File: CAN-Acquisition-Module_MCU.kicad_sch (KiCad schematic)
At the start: 23 parts

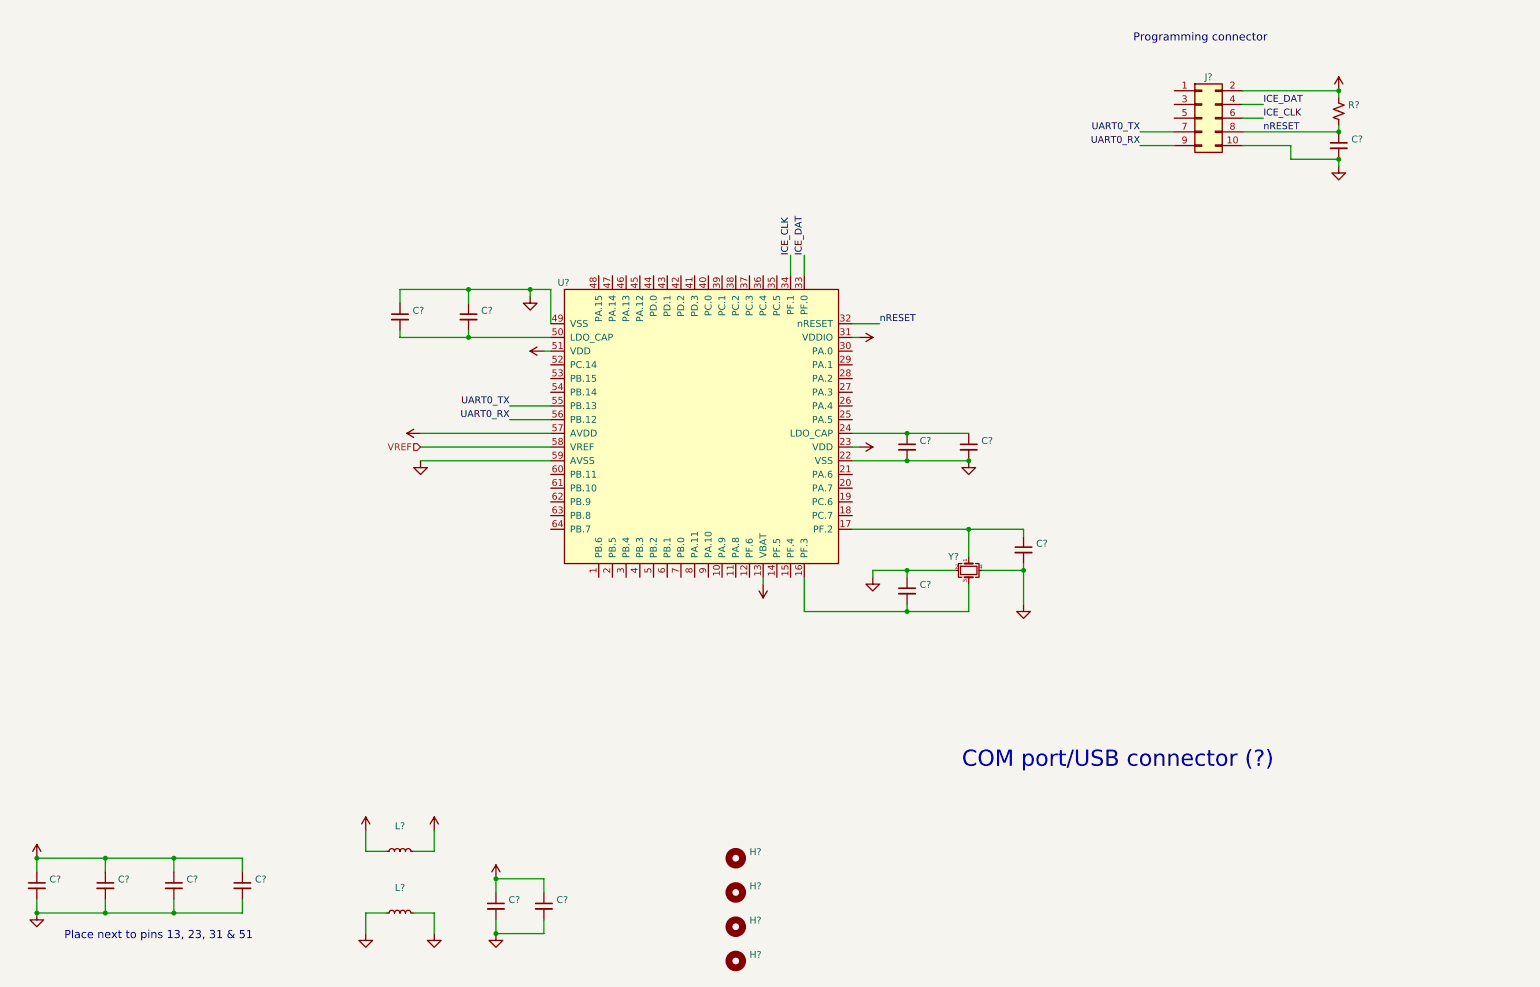
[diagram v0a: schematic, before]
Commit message: Added CAN page
also power section has advanced
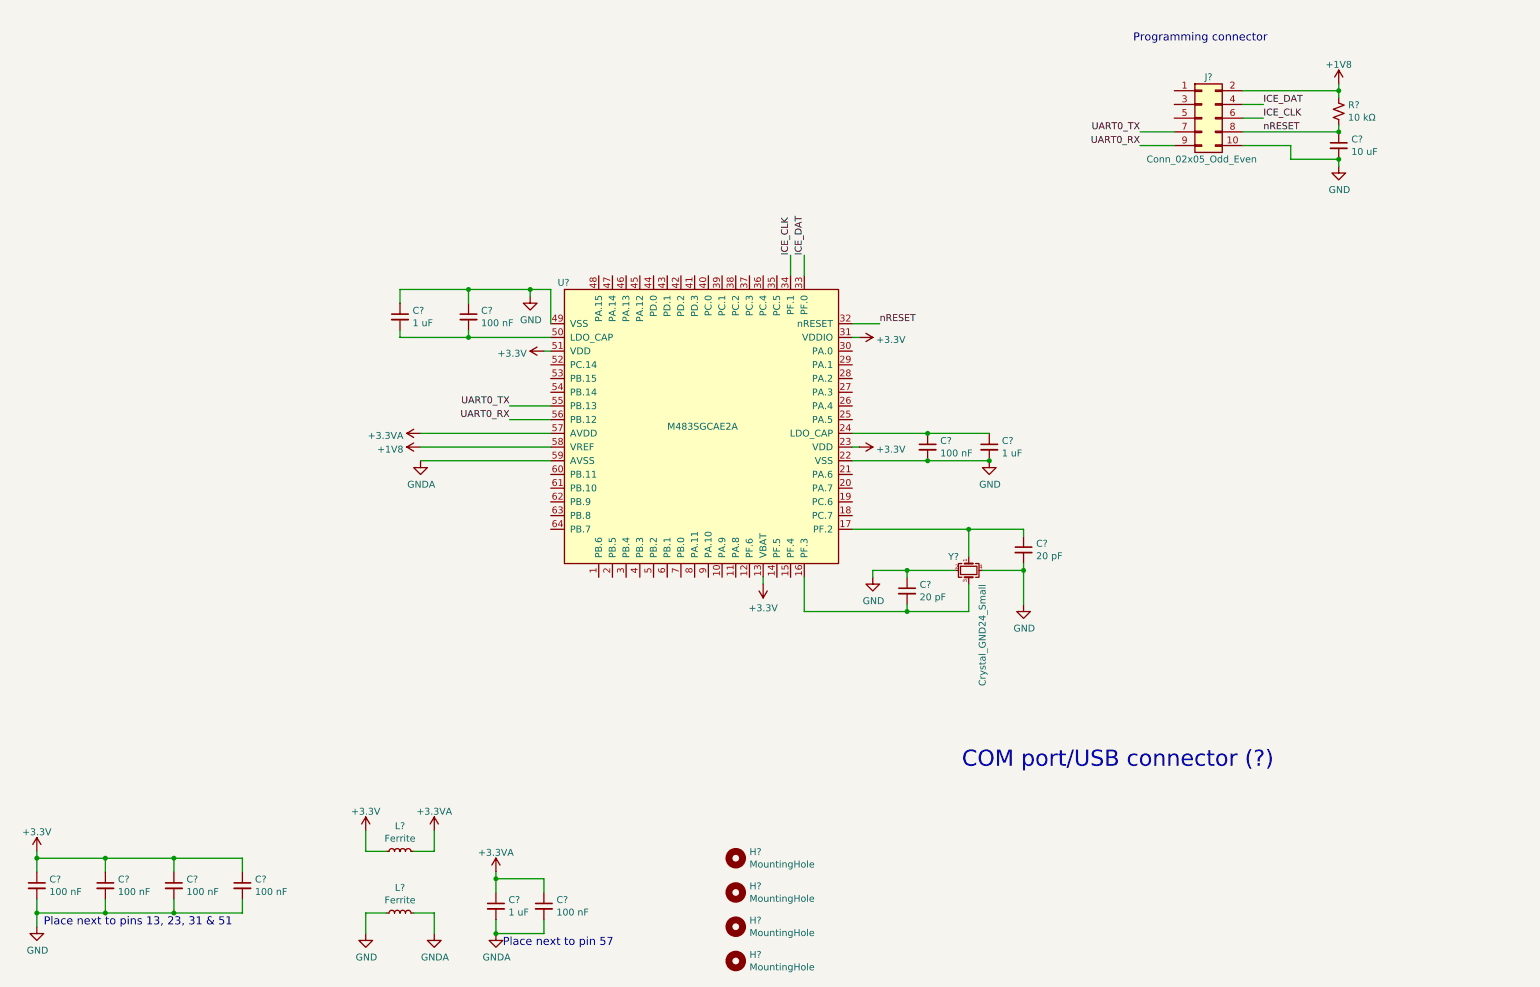
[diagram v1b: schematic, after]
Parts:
- C? (x3): value (none) -> 1 uF; footprint (none) -> Capacitor_SMD:C_0603_1608Metric
- C? (x7): value (none) -> 100 nF; footprint (none) -> Capacitor_SMD:C_0402_1005Metric
- C?: value (none) -> 10 uF; footprint (none) -> Capacitor_SMD:C_1206_3216Metric
- C? (x2): value (none) -> 20 pF; footprint (none) -> Capacitor_SMD:C_0603_1608Metric
- H? (x4): value (none) -> MountingHole
- J?: value (none) -> Conn_02x05_Odd_Even
- L? (x2): value (none) -> Ferrite; footprint (none) -> Inductor_SMD:L_0603_1608Metric
- R?: value (none) -> 10 kΩ; footprint (none) -> Resistor_SMD:R_0603_1608Metric
- U?: value (none) -> M483SGCAE2A; footprint (none) -> Package_QFP:LQFP-64_7x7mm_P0.4mm
- Y?: value (none) -> Crystal_GND24_Small; footprint (none) -> Crystal:Crystal_SMD_3225-4Pin_3.2x2.5mm
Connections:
- net VDD renamed +3V3
- net +3V3: no longer J?.2 (Pin_2), R?.1
- net VDDA renamed +3.3VA
- net VREF renamed +1V8
- net +1V8: now also J?.2 (Pin_2), R?.1
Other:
- note added: "Place next to pin 57"
- moved on the sheet: C?

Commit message: Mid-day backup
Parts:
- added J?: USB_B_Micro, Connector_USB:USB_Micro-B_Wuerth_614105150721_Vertical, symbol Connector:USB_B_Micro
- added L?: Ferrite, Inductor_SMD:L_0603_1608Metric, symbol Device:L_Small
- added R? (x2): 27 Ω, Resistor_SMD:R_0603_1608Metric, symbol Device:R_Small_US
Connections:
- net GND: now also J?.5 (GND), L?.1
- net V_USB: now reaches U?.45 (PA.12)
- net V_USB: now also J?.1 (VBUS)
- net USB_D-: now reaches U?.46 (PA.13)
- net USB_D-: now also R?.2
- net USB_D+: now reaches U?.47 (PA.14)
- net USB_D+: now also R?.2
- net USB_ID: now reaches U?.48 (PA.15)
- net USB_ID: now also J?.4 (ID)
- new net: J?.3 (D+), R?.1
- new net: J?.2 (D-), R?.1
- new net: J?.6 (Shield), L?.2
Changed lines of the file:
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@@
   (junction (at 120.65 66.04) (diameter 0) (color 0 0 0 0)
   )
+  (junction (at 140.97 25.4) (diameter 0) (color 0 0 0 0)
+  )
   (junction (at 114.3 185.42) (diameter 0) (color 0 0 0 0)
   )
@@
     (stroke (width 0) (type default) (color 0 0 0 0))
   )
+  (wire (pts (xy 135.89 30.48) (xy 135.89 38.1))
+    (stroke (width 0) (type default) (color 0 0 0 0))
+  )
   (wire (pts (xy 171.45 119.38) (xy 171.45 125.73))
     (stroke (width 0) (type default) (color 0 0 0 0))
@@
     (stroke (width 0) (type default) (color 0 0 0 0))
   )
+  (wire (pts (xy 128.27 33.02) (xy 138.43 33.02))
+    (stroke (width 0) (type default) (color 0 0 0 0))
+  )
   (wire (pts (xy 29.21 170.18) (xy 29.21 171.45))
     (stroke (width 0) (type default) (color 0 0 0 0))
@@
     (stroke (width 0) (type default) (color 0 0 0 0))
   )
+  (wire (pts (xy 128.27 25.4) (xy 140.97 25.4))
+    (stroke (width 0) (type default) (color 0 0 0 0))
+  )
+  (wire (pts (xy 133.35 63.5) (xy 133.35 35.56))
+    (stroke (width 0) (type default) (color 0 0 0 0))
+  )
   (wire (pts (xy 181.61 95.25) (xy 180.34 95.25))
     (stroke (width 0) (type default) (color 0 0 0 0))
@@
     (stroke (width 0) (type default) (color 0 0 0 0))
   )
+  (wire (pts (xy 140.97 25.4) (xy 140.97 63.5))
+    (stroke (width 0) (type default) (color 0 0 0 0))
+  )
   (wire (pts (xy 212.09 116.84) (xy 212.09 118.11))
     (stroke (width 0) (type default) (color 0 0 0 0))
@@
     (stroke (width 0) (type default) (color 0 0 0 0))
   )
+  (wire (pts (xy 118.11 50.8) (xy 118.11 48.26))
+    (stroke (width 0) (type default) (color 0 0 0 0))
+  )
+  (wire (pts (xy 135.89 43.18) (xy 135.89 63.5))
+    (stroke (width 0) (type default) (color 0 0 0 0))
+  )
   (wire (pts (xy 181.61 74.93) (xy 180.34 74.93))
     (stroke (width 0) (type default) (color 0 0 0 0))
@@
     (stroke (width 0) (type default) (color 0 0 0 0))
   )
+  (wire (pts (xy 140.97 22.86) (xy 140.97 25.4))
+    (stroke (width 0) (type default) (color 0 0 0 0))
+  )
   (wire (pts (xy 261.62 41.91) (xy 270.51 41.91))
     (stroke (width 0) (type default) (color 0 0 0 0))
@@
     (stroke (width 0) (type default) (color 0 0 0 0))
   )
+  (wire (pts (xy 133.35 35.56) (xy 128.27 35.56))
+    (stroke (width 0) (type default) (color 0 0 0 0))
+  )
+  (wire (pts (xy 118.11 43.18) (xy 118.11 40.64))
+    (stroke (width 0) (type default) (color 0 0 0 0))
+  )
   (wire (pts (xy 270.51 35.56) (xy 270.51 36.83))
     (stroke (width 0) (type default) (color 0 0 0 0))
@@
     (stroke (width 0) (type default) (color 0 0 0 0))
   )
+  (wire (pts (xy 138.43 49.53) (xy 138.43 63.5))
+    (stroke (width 0) (type default) (color 0 0 0 0))
+  )
   (wire (pts (xy 96.52 68.58) (xy 96.52 66.04))
     (stroke (width 0) (type default) (color 0 0 0 0))
@@
     (stroke (width 0) (type default) (color 0 0 0 0))
   )
+  (wire (pts (xy 128.27 30.48) (xy 135.89 30.48))
+    (stroke (width 0) (type default) (color 0 0 0 0))
+  )
   (wire (pts (xy 171.45 63.5) (xy 171.45 59.69))
     (stroke (width 0) (type default) (color 0 0 0 0))
@@
   )
   (wire (pts (xy 123.19 177.8) (xy 123.19 175.26))
+    (stroke (width 0) (type default) (color 0 0 0 0))
+  )
+  (wire (pts (xy 138.43 33.02) (xy 138.43 44.45))
     (stroke (width 0) (type default) (color 0 0 0 0))
   )
@@
     (effects (font (size 1.27 1.27)) (justify left bottom))
   )
+  (label "USB_VBUS" (at 140.97 60.96 90)
+    (effects (font (size 1.27 1.27)) (justify left bottom))
+  )
   (label "ICE_DAT" (at 256.54 31.75 0)
     (effects (font (size 1.27 1.27)) (justify left bottom))
@@
     (effects (font (size 1.27 1.27)) (justify left bottom))
   )
+  (label "USB_ID" (at 133.35 60.96 90)
+    (effects (font (size 1.27 1.27)) (justify left bottom))
+  )
+  (label "USB_D+" (at 135.89 60.96 90)
+    (effects (font (size 1.27 1.27)) (justify left bottom))
+  )
   (label "ICE_CLK" (at 256.54 34.29 0)
     (effects (font (size 1.27 1.27)) (justify left bottom))
   )
+  (label "USB_D-" (at 138.43 60.96 90)
+    (effects (font (size 1.27 1.27)) (justify left bottom))
+  )
   (label "nRESET" (at 185.42 72.39 0)
     (effects (font (size 1.27 1.27)) (justify left bottom))
@@
   (label "UART0_TX" (at 233.68 36.83 180)
     (effects (font (size 1.27 1.27)) (justify right bottom))
+  )
+  (hierarchical_label "V_USB" (shape input) (at 140.97 22.86 90)
+    (effects (font (size 1.27 1.27)) (justify left))
   )
   (symbol (lib_id "CAN-Acquisition-Module-rescue:M483SGCAE2A-CAN-Acquisition-Module") (at 127 66.04 0) (unit 1)
@@
     (pin "1")
   )
+  (symbol (lib_id "Device:R_Small_US") (at 135.89 40.64 0) (unit 1)
+    (in_bom yes) (on_board yes)
+    (property "Reference" "R?" (id 0) (at 135.89 43.18 0)
+      (effects (font (size 1.27 1.27)) (justify left))
+    )
+    (property "Value" "27 Ω" (id 1) (at 137.16 38.1 90)
+      (effects (font (size 1.27 1.27)) (justify left))
+    )
+    (property "Footprint" "Resistor_SMD:R_0603_1608Metric" (id 2) (at 135.89 40.64 0)
+      (effects (font (size 1.27 1.27)) hide)
+    )
+    (property "Datasheet" "~" (id 3) (at 135.89 40.64 0)
+      (effects (font (size 1.27 1.27)) hide)
+    )
+    (pin "1")
+    (pin "2")
+  )
+  (symbol (lib_id "Connector:USB_B_Micro") (at 120.65 30.48 0) (unit 1)
+    (in_bom yes) (on_board yes) (fields_autoplaced)
+    (property "Reference" "J?" (id 0) (at 120.65 19.1602 0))
+    (property "Value" "USB_B_Micro" (id 1) (at 120.65 21.6971 0))
+    (property "Footprint" "Connector_USB:USB_Micro-B_Wuerth_614105150721_Vertical" (id 2) (at 124.46 31.75 0)
+      (effects (font (size 1.27 1.27)) hide)
+    )
+    (property "Datasheet" "https://gct.co/files/drawings/usb3131.pdf?v=33e528c4-fc40-4e86-8db1-6ee6a219205e" (id 3) (at 124.46 31.75 0)
+      (effects (font (size 1.27 1.27)) hide)
+    )
+    (property "Alternate Mfr." "GCT" (id 4) (at 120.65 30.48 0)
+      (effects (font (size 1.27 1.27)) hide)
+    )
+    (property "Alternate P/N" "USB3131-30-0230-A" (id 5) (at 120.65 30.48 0)
+      (effects (font (size 1.27 1.27)) hide)
+    )
+    (pin "1")
+    (pin "2")
+    (pin "3")
+    (pin "4")
+    (pin "5")
+    (pin "6")
+  )
   (symbol (lib_id "power:+1V8") (at 270.51 27.94 0) (unit 1)
     (in_bom yes) (on_board yes) (fields_autoplaced)
@@
     (pin "1")
   )
+  (symbol (lib_id "power:GND") (at 118.11 50.8 0) (unit 1)
+    (in_bom yes) (on_board yes)
+    (property "Reference" "#PWR?" (id 0) (at 118.11 57.15 0)
+      (effects (font (size 1.27 1.27)) hide)
+    )
+    (property "Value" "GND" (id 1) (at 116.84 54.61 0))
+    (property "Footprint" "" (id 2) (at 118.11 50.8 0)
+      (effects (font (size 1.27 1.27)) hide)
+    )
+    (property "Datasheet" "" (id 3) (at 118.11 50.8 0)
+      (effects (font (size 1.27 1.27)) hide)
+    )
+    (pin "1")
+  )
+  (symbol (lib_id "power:GND") (at 120.65 40.64 0) (unit 1)
+    (in_bom yes) (on_board yes)
+    (property "Reference" "#PWR?" (id 0) (at 120.65 46.99 0)
+      (effects (font (size 1.27 1.27)) hide)
+    )
+    (property "Value" "GND" (id 1) (at 120.65 44.45 0))
+    (property "Footprint" "" (id 2) (at 120.65 40.64 0)
+      (effects (font (size 1.27 1.27)) hide)
+    )
+    (property "Datasheet" "" (id 3) (at 120.65 40.64 0)
+      (effects (font (size 1.27 1.27)) hide)
+    )
+    (pin "1")
+  )
   (symbol (lib_id "power:+3.3VA") (at 102.87 166.37 0) (unit 1)
     (in_bom yes) (on_board yes) (fields_autoplaced)
@@
     (pin "1")
   )
+  (symbol (lib_id "Device:L_Small") (at 118.11 45.72 180) (unit 1)
+    (in_bom yes) (on_board yes)
+    (property "Reference" "L?" (id 0) (at 113.411 45.72 90))
+    (property "Value" "Ferrite" (id 1) (at 115.7224 45.72 90))
+    (property "Footprint" "Inductor_SMD:L_0603_1608Metric" (id 2) (at 118.11 45.72 0)
+      (effects (font (size 1.27 1.27)) hide)
+    )
+    (property "Datasheet" "~" (id 3) (at 118.11 45.72 0)
+      (effects (font (size 1.27 1.27)) hide)
+    )
+    (pin "1")
+    (pin "2")
+  )
+  (symbol (lib_id "Device:R_Small_US") (at 138.43 46.99 0) (unit 1)
+    (in_bom yes) (on_board yes)
+    (property "Reference" "R?" (id 0) (at 138.43 49.53 0)
+      (effects (font (size 1.27 1.27)) (justify left))
+    )
+    (property "Value" "27 Ω" (id 1) (at 139.7 44.45 90)
+      (effects (font (size 1.27 1.27)) (justify left))
+    )
+    (property "Footprint" "Resistor_SMD:R_0603_1608Metric" (id 2) (at 138.43 46.99 0)
+      (effects (font (size 1.27 1.27)) hide)
+    )
+    (property "Datasheet" "~" (id 3) (at 138.43 46.99 0)
+      (effects (font (size 1.27 1.27)) hide)
+    )
+    (pin "1")
+    (pin "2")
+  )
 )

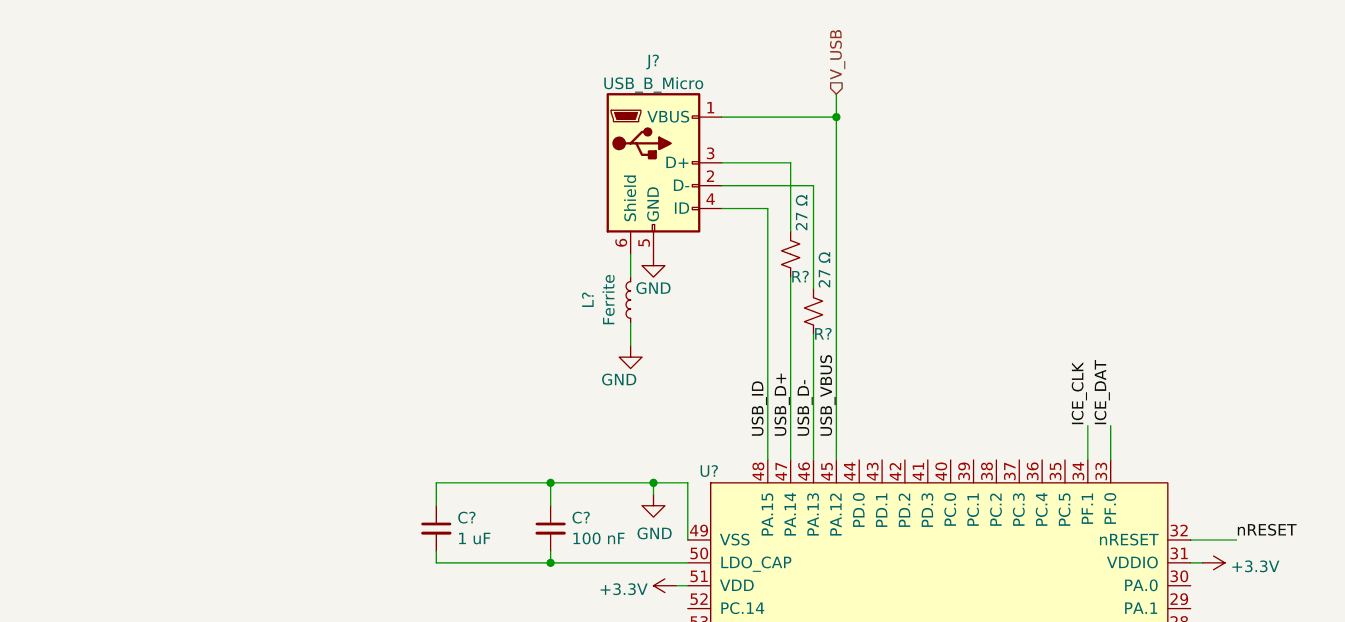
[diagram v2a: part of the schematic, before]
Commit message: Advanced CAN section and "finished" power section
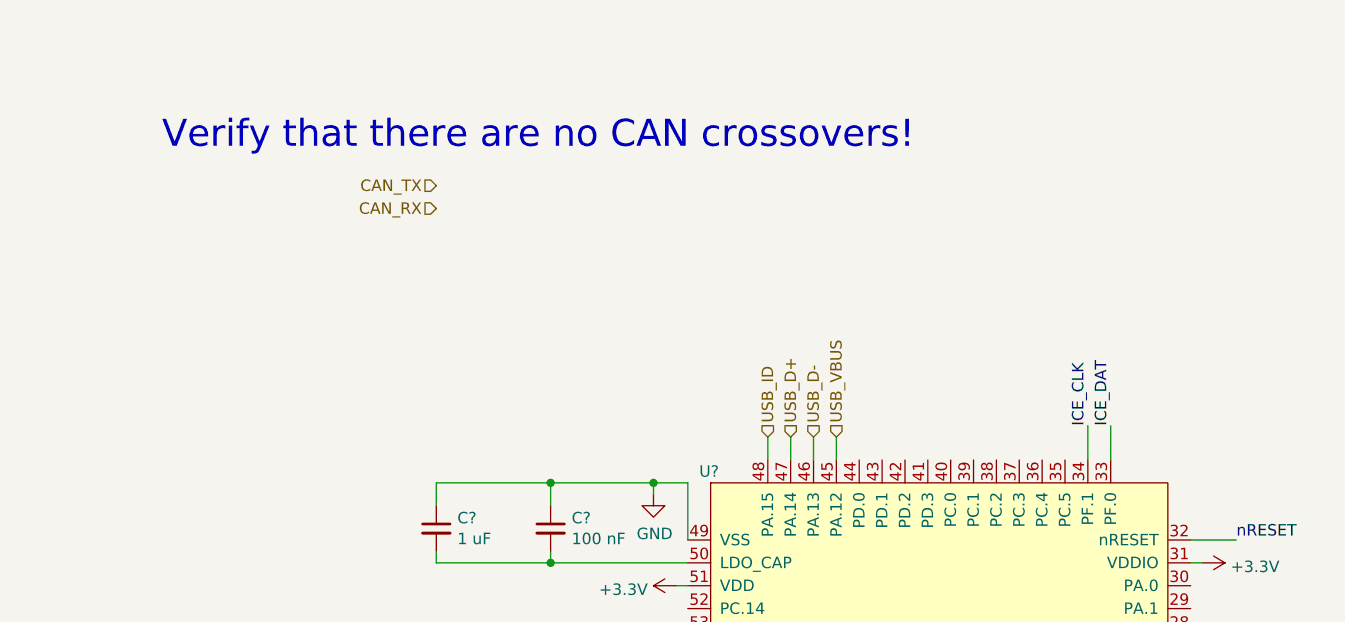
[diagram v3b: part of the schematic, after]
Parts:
- removed J?: USB_B_Micro, Connector_USB:USB_Micro-B_Wuerth_614105150721_Vertical, symbol Connector:USB_B_Micro
- removed L?: Ferrite, Inductor_SMD:L_0603_1608Metric, symbol Device:L_Small
- removed R? (x2): 27 Ω, Resistor_SMD:R_0603_1608Metric, symbol Device:R_Small_US
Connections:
- net V_USB renamed USB_VBUS
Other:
- note added: "Verify that there are no CAN crossovers!"
